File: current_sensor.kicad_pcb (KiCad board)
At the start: 2 copper layers, 27.9 x 40.6 mm, 5 parts, among them J1 XT_60, J2 XT_60, J3 Conn_01x03_Male, U1 ACS781xLRTR-100B

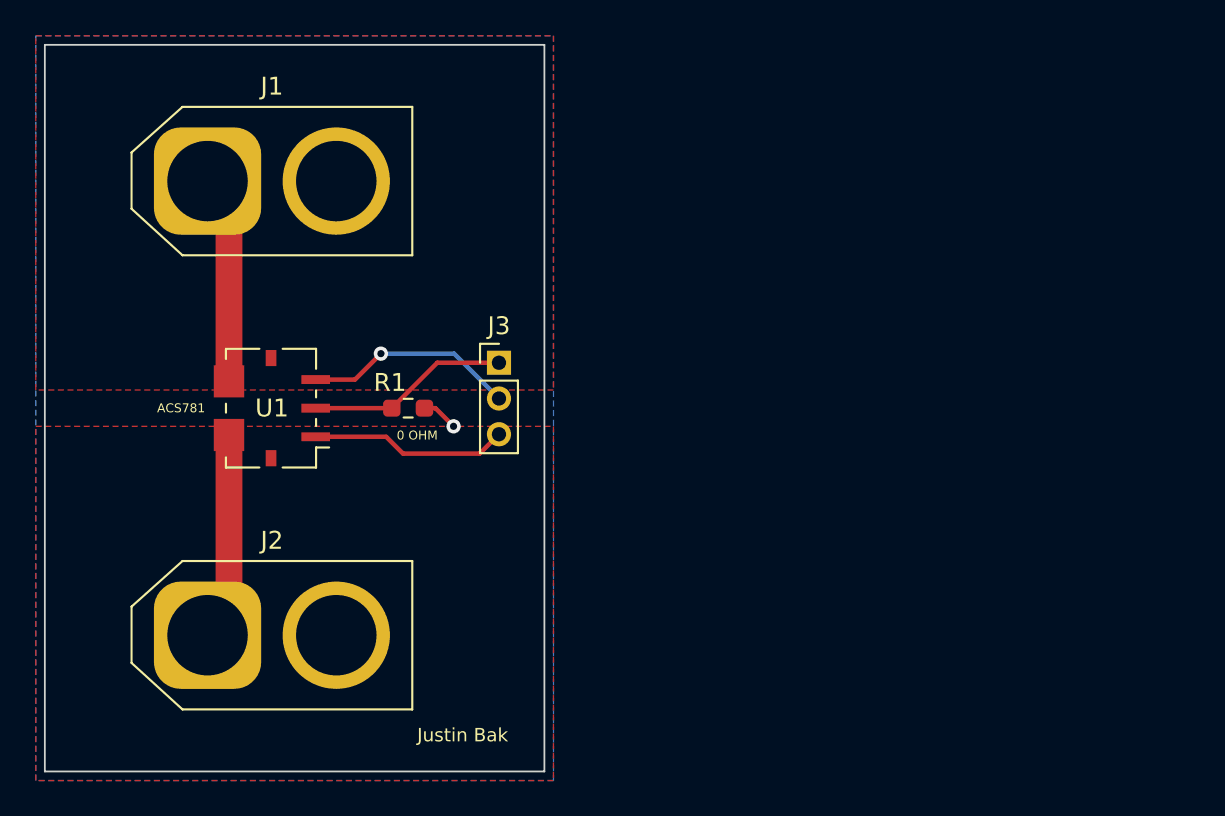
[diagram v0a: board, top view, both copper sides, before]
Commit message: making it much smaller
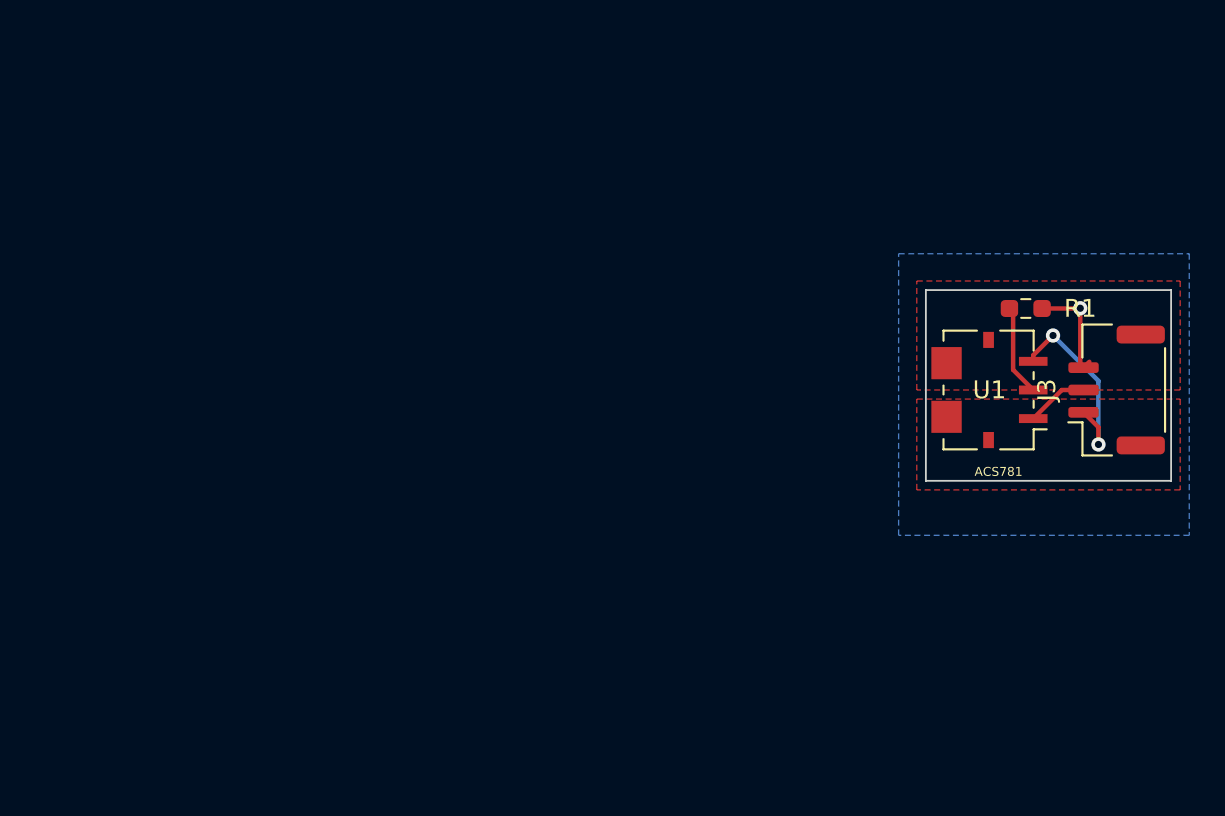
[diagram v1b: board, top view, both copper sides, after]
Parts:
- removed J1: XT_60, Connector_AMASS:AMASS_XT60-F_1x02_P7.20mm_Vertical
- removed J2: XT_60, Connector_AMASS:AMASS_XT60-M_1x02_P7.20mm_Vertical
- J3: footprint Connector_PinHeader_2.00mm:PinHeader_1x03_P2.00mm_Vertical -> Connector_Molex:Molex_CLIK-Mate_502386-0370_1x03-1MP_P1.25mm_Horizontal
- R1: value 0Ohm -> R
- moved U1 40.1 mm to (207.8, 87.9)
- moved R1 35.0 mm to (209.8, 83.3), turned to 180 degrees
- moved J3 34.6 mm to (214.9, 87.9), turned to 90 degrees
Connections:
- J3 pad 2: Net-(J3-Pad2) -> +3.3V
- J3 pad 3: Net-(J3-Pad3) -> GND
- R1 pad 1: Net-(J3-Pad1) -> GND
- R1 pad 2: GND -> Net-(R1-Pad2)
- U1 pad 1: Net-(J3-Pad3) -> +3.3V
- U1 pad 2: Net-(J3-Pad1) -> Net-(R1-Pad2)
- U1 pad 3: Net-(J3-Pad2) -> Net-(J3-Pad1)
- U1 pad 5: Net-(J1-Pad1) -> +12V
- U1 pad 6: Net-(J2-Pad1) -> -12V
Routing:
- net Net-(J3-Pad2): track 11.9 -> 0.00 mm, vias 1 -> 0
- net Net-(J1-Pad1): track 11.7 -> 0.00 mm
- net Net-(J2-Pad1): track 11.7 -> 0.00 mm
- net Net-(J3-Pad3): track 11.1 -> 0.00 mm
- net Net-(R1-Pad2): track 0.00 -> 5.24 mm
- net GND: track 2.15 -> 6.00 mm
- net +3.3V: track 0.00 -> 3.47 mm
- net Net-(J3-Pad1): track 11.3 -> 11.2 mm, vias 0 -> 2
- added copper zone on F.Cu, net +12V
- added copper zone on F.Cu, net -12V
- removed copper zone on F.Cu, net Net-(J1-Pad1)
- removed copper zone on F.Cu, net Net-(J2-Pad1)
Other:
- board size 27.9 x 40.6 mm -> 13.7 x 10.7 mm
- board text removed: "0 OHM"

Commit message: make it smaller
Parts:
- added C1: 0.1 uF, Capacitor_SMD:C_0603_1608Metric_Pad1.08x0.95mm_HandSolder, F.Cu at (212.9, 89.9)
- added C2: Cf, Capacitor_SMD:C_0603_1608Metric_Pad1.08x0.95mm_HandSolder, F.Cu at (212.9, 83.8)
- J3: footprint Connector_Molex:Molex_CLIK-Mate_502386-0370_1x03-1MP_P1.25mm_Horizontal -> Connector_Molex:Molex_PicoBlade_53261-0371_1x03-1MP_P1.25mm_Horizontal; moved to B.Cu
- R1: value R -> Rf
- moved J3 4.60 mm to (210.3, 88.4), turned to -90 degrees
- moved R1 4.30 mm to (212.9, 86.4), turned to 90 degrees
- moved U1 1.14 mm to (207.3, 88.9)
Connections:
- J3 pad 3: GND -> GNDREF
- R1 pad 1: GND -> Net-(U1-Pad3)
- R1 pad 2: Net-(R1-Pad2) -> Net-(J3-Pad1)
- U1 pad 2: Net-(R1-Pad2) -> GNDREF
- U1 pad 3: Net-(J3-Pad1) -> Net-(U1-Pad3)
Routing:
- net GNDREF: track 0.00 -> 7.42 mm, vias 0 -> 2
- net GND: track 6.00 -> 0.00 mm, vias 1 -> 0
- net +3.3V: track 3.47 -> 9.27 mm, vias 0 -> 1
- net Net-(R1-Pad2): track 5.24 -> 0.00 mm
- net Net-(J3-Pad1): track 11.2 -> 7.63 mm, vias 2 -> 1
- net Net-(U1-Pad3): track 0.00 -> 3.15 mm
- net -12V: vias 0 -> 8
- net +12V: vias 0 -> 7
- added copper zone on B.Cu, net GNDREF
- removed copper zone on B.Cu, net GND
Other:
- board size 13.7 x 10.7 mm -> 14.7 x 12.2 mm
